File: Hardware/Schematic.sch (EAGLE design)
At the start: 46 parts, among them IC1 XC6220A331MR-G, J1 SAMACSYS_PARTS_USB4110-GF-A, J2 FH34SRJ-24S-0.5SH_99_, J4 112A-TAAR-R03_ATTEND, Q1 20V/4.2A/52mΩ/1.4W, Q2 SI1308EDL-T1-GE3, U1 ESP32_WROVER_SPARKFUN-IC-POWE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, U2 ESP32-C6-WROOM-1-N8

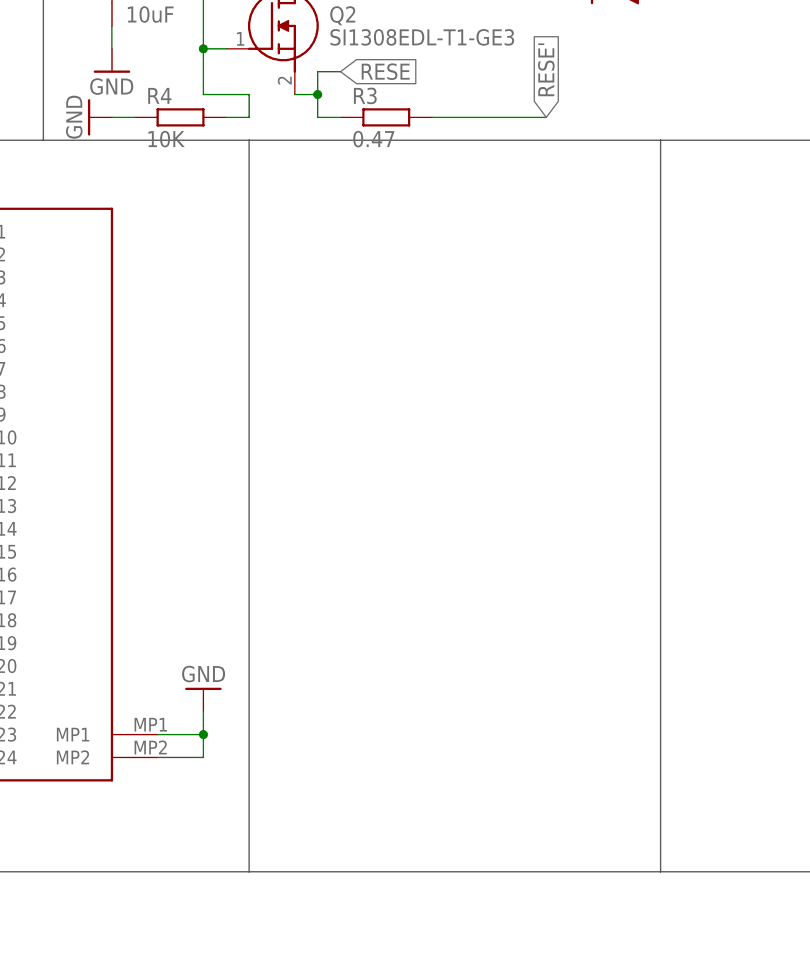
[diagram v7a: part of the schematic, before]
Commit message: add EPD Power
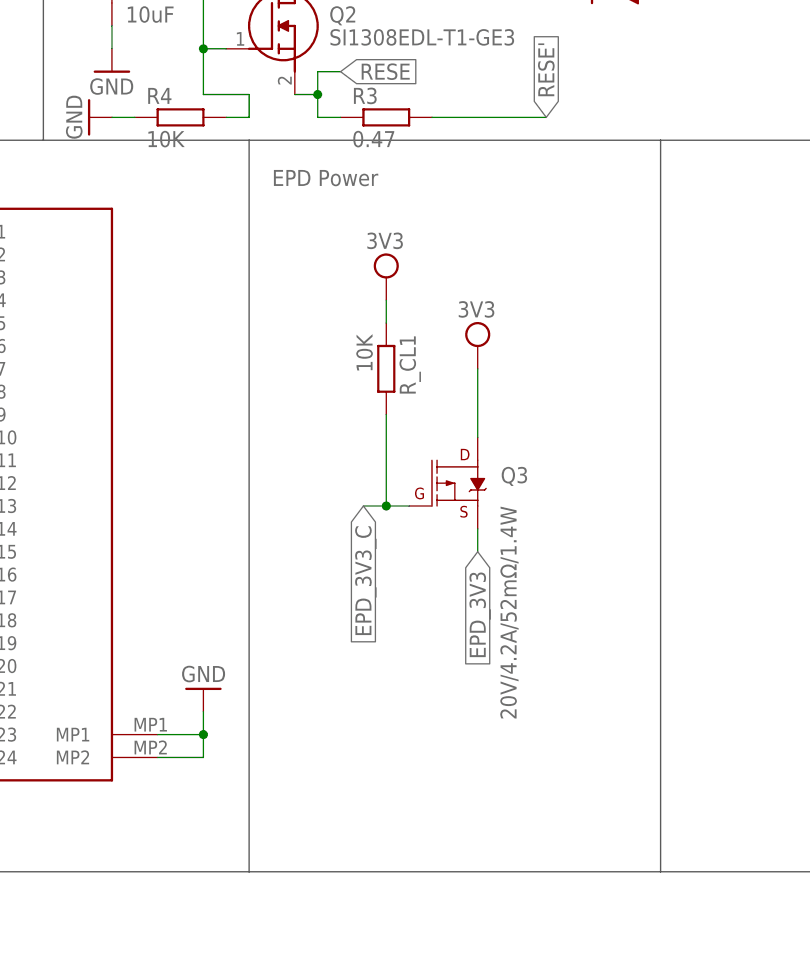
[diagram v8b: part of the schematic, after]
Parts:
- added Q3: 20V/4.2A/52mΩ/1.4W, DeskAssistant v19 v1.flbr:ESP32_WROVER_SPARKFUN-DISCRETESEMI_MOSFET_PCH-DMG2305UX-7
- added R_CL1: 10K, DeskAssistant v19 v1.flbr:ESP32_WROVER_EAGLE-LTSPICE_RR0402
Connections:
- net 3V3: now also Q3.D, R_CL1.1
- net EPD_3V3: now also Q3.S
- net EPD_3V3_C: now also Q3.G, R_CL1.2
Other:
- note added: "EPD Power"
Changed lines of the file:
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@@
 <part name="GND25" library="DeskAssistant v19 v1.flbr" library_urn="urn:adsk.wipprod:fs.file:vf.vVvdDOfaSfavM5thX5SjWw" deviceset="GND" device=""/>
 <part name="GND26" library="DeskAssistant v19 v1.flbr" library_urn="urn:adsk.wipprod:fs.file:vf.vVvdDOfaSfavM5thX5SjWw" deviceset="GND" device=""/>
+<part name="Q3" library="DeskAssistant v19 v1.flbr" library_urn="urn:adsk.wipprod:fs.file:vf.vVvdDOfaSfavM5thX5SjWw" deviceset="ESP32_WROVER_SPARKFUN-DISCRETESEMI_MOSFET_PCH" device="-DMG2305UX-7" value="20V/4.2A/52mΩ/1.4W"/>
+<part name="SUPPLY5" library="DeskAssistant v19 v1.flbr" library_urn="urn:adsk.wipprod:fs.file:vf.vVvdDOfaSfavM5thX5SjWw" deviceset="3V3-CIRCLE" device="" value="3V3"/>
+<part name="SUPPLY6" library="DeskAssistant v19 v1.flbr" library_urn="urn:adsk.wipprod:fs.file:vf.vVvdDOfaSfavM5thX5SjWw" deviceset="3V3-CIRCLE" device="" value="3V3"/>
+<part name="R_CL1" library="DeskAssistant v19 v1.flbr" library_urn="urn:adsk.wipprod:fs.file:vf.vVvdDOfaSfavM5thX5SjWw" deviceset="ESP32_WROVER_EAGLE-LTSPICE_R" device="R0402" value="10K"/>
 </parts>
 <sheets>
@@
 <text x="124.46" y="228.6" size="1.778" layer="95" align="center">ESP32 C6</text>
 <text x="-160.02" y="165.1" size="1.778" layer="95">E-Paper Display Header</text>
+<text x="-73.66" y="162.56" size="1.778" layer="95">EPD Power</text>
 </plain>
 <instances>
@@
 <instance part="GND26" gate="1" x="-157.48" y="129.54" smashed="yes" rot="R180">
 <attribute name="VALUE" x="-154.94" y="132.08" size="1.778" layer="96" rot="R180"/>
+</instance>
+<instance part="Q3" gate="G$1" x="-53.34" y="129.54" smashed="yes">
+<attribute name="NAME" x="-48.26" y="129.54" size="1.778" layer="95" font="vector"/>
+<attribute name="VALUE" x="-48.26" y="127" size="1.778" layer="96" font="vector" rot="R270"/>
+</instance>
+<instance part="SUPPLY5" gate="G$1" x="-50.8" y="144.78" smashed="yes">
+<attribute name="VALUE" x="-50.927" y="147.955" size="1.778" layer="96" align="bottom-center"/>
+</instance>
+<instance part="SUPPLY6" gate="G$1" x="-60.96" y="152.4" smashed="yes">
+<attribute name="VALUE" x="-61.087" y="155.575" size="1.778" layer="96" align="bottom-center"/>
+</instance>
+<instance part="R_CL1" gate="G$1" x="-60.96" y="142.24" smashed="yes" rot="R270">
+<attribute name="NAME" x="-59.4614" y="146.05" size="1.778" layer="95" rot="R270"/>
+<attribute name="VALUE" x="-64.262" y="146.05" size="1.778" layer="96" rot="R270"/>
+<attribute name="NAME" x="-59.4614" y="146.05" size="1.778" layer="95" rot="R270"/>
+<attribute name="VALUE" x="-64.262" y="146.05" size="1.778" layer="96" rot="R270"/>
 </instance>
 </instances>
@@
 <pinref part="SUPPLY4" gate="G$1" pin="3V3"/>
 </segment>
+<segment>
+<pinref part="Q3" gate="G$1" pin="D"/>
+<wire x1="-50.8" y1="134.62" x2="-50.8" y2="142.24" width="0.1524" layer="91"/>
+<pinref part="SUPPLY5" gate="G$1" pin="3V3"/>
+</segment>
+<segment>
+<pinref part="SUPPLY6" gate="G$1" pin="3V3"/>
+<pinref part="R_CL1" gate="G$1" pin="1"/>
+<wire x1="-60.96" y1="149.86" x2="-60.96" y2="147.32" width="0.1524" layer="91"/>
+</segment>
 </net>
 <net name="N$3" class="0">
@@
 <junction x="-114.3" y="119.38"/>
 <label x="-116.84" y="119.38" size="1.778" layer="95" rot="R180" xref="yes"/>
+</segment>
+<segment>
+<pinref part="Q3" gate="G$1" pin="S"/>
+<wire x1="-50.8" y1="124.46" x2="-50.8" y2="121.92" width="0.1524" layer="91"/>
+<label x="-50.8" y="121.92" size="1.778" layer="95" rot="R270" xref="yes"/>
 </segment>
 </net>
@@
 <label x="190.5" y="193.04" size="1.778" layer="95" xref="yes"/>
 </segment>
-</net>
+<segment>
+<pinref part="Q3" gate="G$1" pin="G"/>
+<wire x1="-58.42" y1="127" x2="-60.96" y2="127" width="0.1524" layer="91"/>
+<label x="-63.5" y="127" size="1.778" layer="95" rot="R270" xref="yes"/>
+<wire x1="-60.96" y1="127" x2="-63.5" y2="127" width="0.1524" layer="91"/>
+<junction x="-60.96" y="127"/>
+<wire x1="-60.96" y1="127" x2="-60.96" y2="137.16" width="0.1524" layer="91"/>
+<pinref part="R_CL1" gate="G$1" pin="2"/>
+</segment>
+</net>
